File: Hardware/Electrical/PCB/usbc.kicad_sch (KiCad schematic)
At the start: 14 parts, among them J1 USB_C_Receptacle_USB2.0_14P, U1 TPS25730D, U3 USBLC6-2SC6

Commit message: project state at start of school project
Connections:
- net LDO_1V5: now also U1.3 (ADCIN2)
- net LDO_3V3: no longer U1.3 (ADCIN2)
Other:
- note added: "Max Voltage 15V"
- note removed: "Max Voltage 20V"
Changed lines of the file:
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@@
 		)
 	)
-	(text "Max Voltage 20V"
+	(text "Max Voltage 15V"
 		(exclude_from_sim no)
 		(at 104.902 105.664 0)
@@
 		)
 	)
-	(global_label "LDO_3V3"
+	(global_label "LDO_1V5"
 		(shape input)
 		(at 125.73 105.41 180)

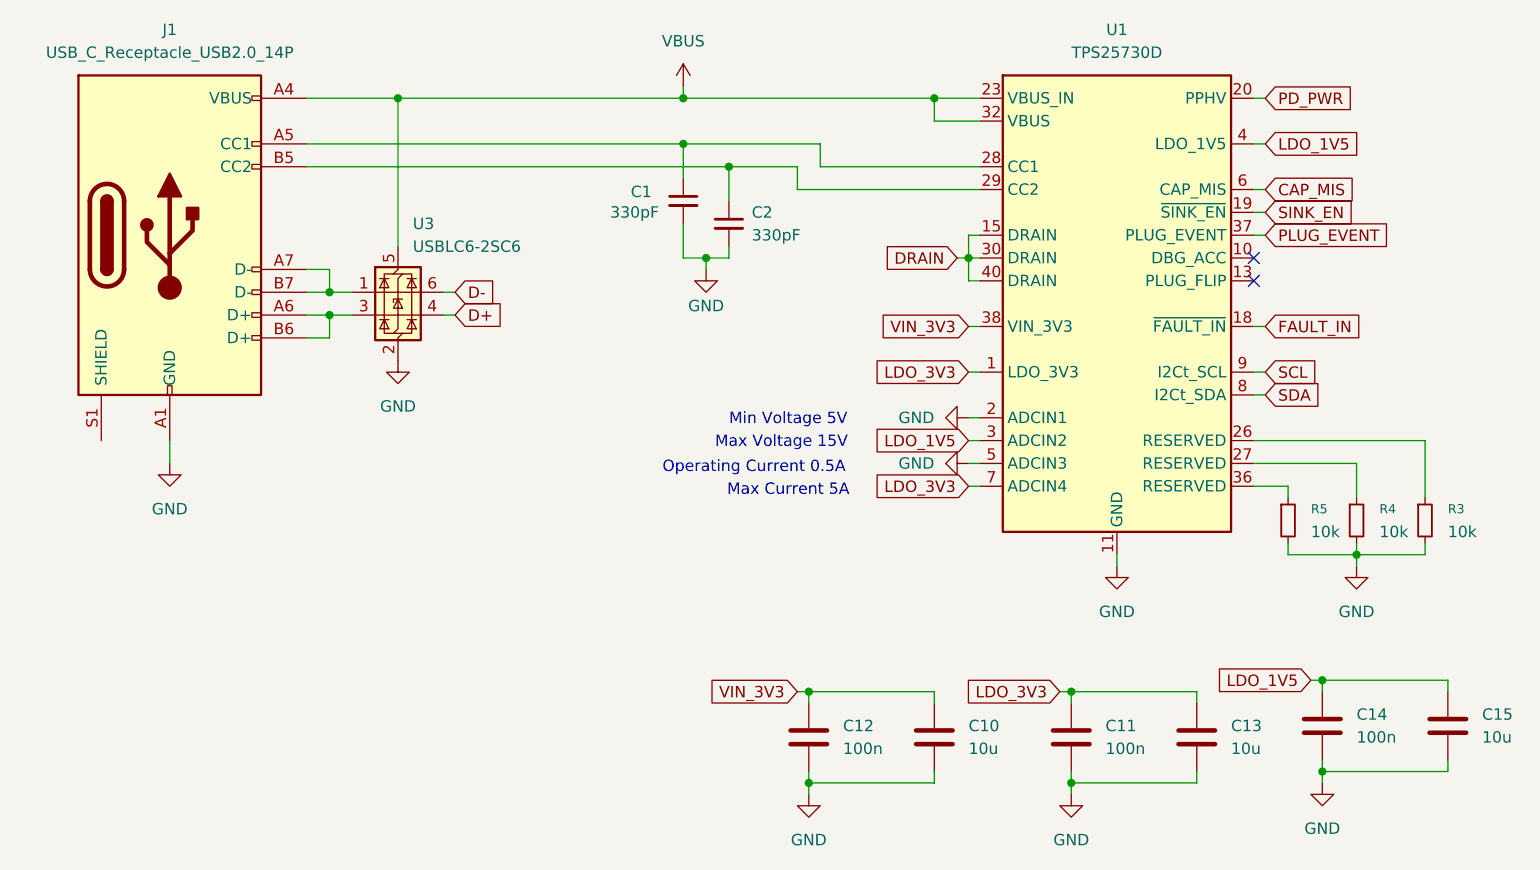
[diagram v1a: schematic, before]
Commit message: Basic Schematic finished, external connectors missing, no footprints or LCSC numbers yet
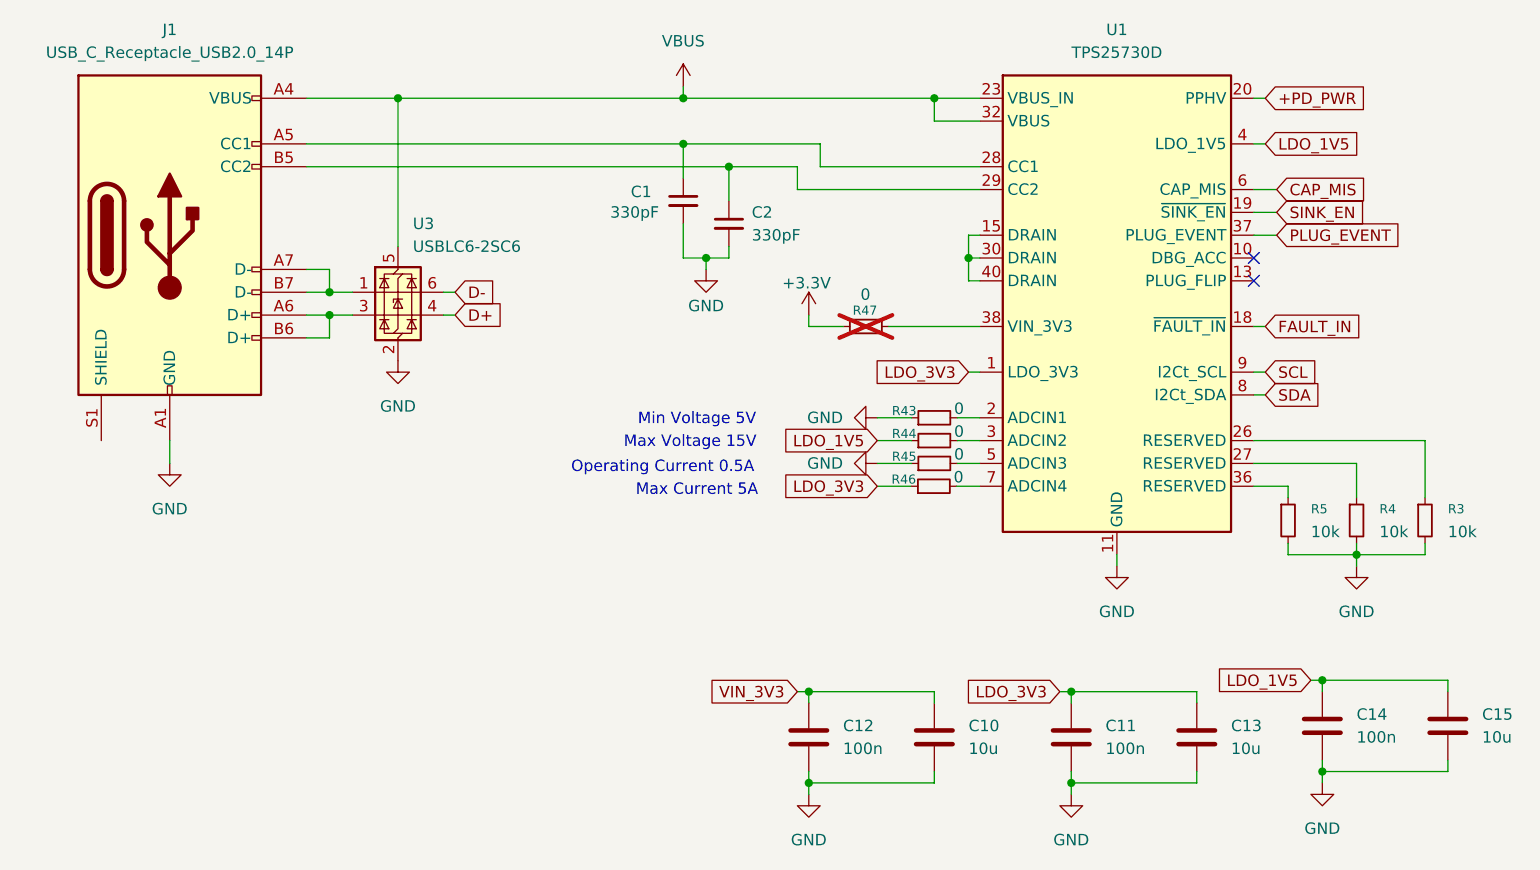
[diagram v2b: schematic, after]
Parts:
- added R43, R44, R45, R46, R47: 0, symbol Device:R_Small
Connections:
- net GND: now also R43.1, R45.1; no longer U1.2 (ADCIN1), U1.5 (ADCIN3)
- net LDO_1V5: now also R44.1; no longer U1.3 (ADCIN2)
- net LDO_3V3: now also R46.1; no longer U1.7 (ADCIN4)
- net VIN_3V3: no longer U1.38 (VIN_3V3)
- net DRAIN: no longer names the net of U1.15 (DRAIN), U1.30 (DRAIN), U1.40 (DRAIN)
- net PD_PWR renamed +PD_PWR
- new net: R47.2, U1.38 (VIN_3V3)
- new net: R46.2, U1.7 (ADCIN4)
- new net: R43.2, U1.2 (ADCIN1)
- new net: R44.2, U1.3 (ADCIN2)
- new net: R45.2, U1.5 (ADCIN3)
- new net +3.3V: R47.1

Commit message: layout v1 finished but not confirmed yet
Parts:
- removed C13, C15: 10u, symbol Device:C
- removed J1: USB_C_Receptacle_USB2.0_14P, Connector_USB:USB_C_Receptacle_HRO_TYPE-C-31-M-17, symbol Connector:USB_C_Receptacle_USB2.0_14P
- added J1: USB_C_Receptacle_USB2.0_16P, Connector_USB:USB_C_Receptacle_G-Switch_GT-USB-7010ASV, symbol Connector:USB_C_Receptacle_USB2.0_16P
- C1, C2: footprint (none) -> Capacitor_SMD:C_0603_1608Metric; *LCSC Part Number (none) -> C1664
- C10: footprint (none) -> Capacitor_SMD:C_1206_3216Metric; *LCSC Part Number (none) -> C13585
- C11, C12, C14: footprint (none) -> Capacitor_SMD:C_0603_1608Metric; *LCSC Part Number (none) -> C14663
- R3, R4, R5: footprint (none) -> Resistor_SMD:R_0603_1608Metric; *LCSC Part Number (none) -> C25804
- R43, R44, R45, R46: footprint (none) -> Resistor_SMD:R_0603_1608Metric; *LCSC Part Number (none) -> C21189
- R47: footprint (none) -> Resistor_SMD:R_0603_1608Metric
- U1: *LCSC Part Number (none) -> C22438973
- U3: *LCSC Part Number (none) -> USBLC6-2SC6
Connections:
- net VIN_3V3 is gone; now on net +3.3V: C10.1, C12.1
- net GND: now also J1.A1 (GND), J1.A12 (GND), J1.B1 (GND), J1.B12 (GND)
- net VBUS: now also J1.A4 (VBUS), J1.A9 (VBUS), J1.B4 (VBUS), J1.B9 (VBUS)
- net at C1.1, U1.28 (CC1): now also J1.A5 (CC1)
- net at U3.3 (I/O2): now also J1.A6 (D+), J1.B6 (D+)
- net at U3.1 (I/O1): now also J1.A7 (D-), J1.B7 (D-)
- net at C2.1, U1.29 (CC2): now also J1.B5 (CC2)
- no-connect marks 2 -> 5
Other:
- moved on the sheet: U3
